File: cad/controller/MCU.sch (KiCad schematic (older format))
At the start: 37 parts, among them J3 Conn_02x03_Odd_Even, J4 Conn_01x02, J5 Conn_01x04, J6 Conn_01x05, J7 6P6C, SW2 SW_Push, U5 ATmega328-PU, U6 PCA9517A, U7 TXB0104D, Y2 18MHz

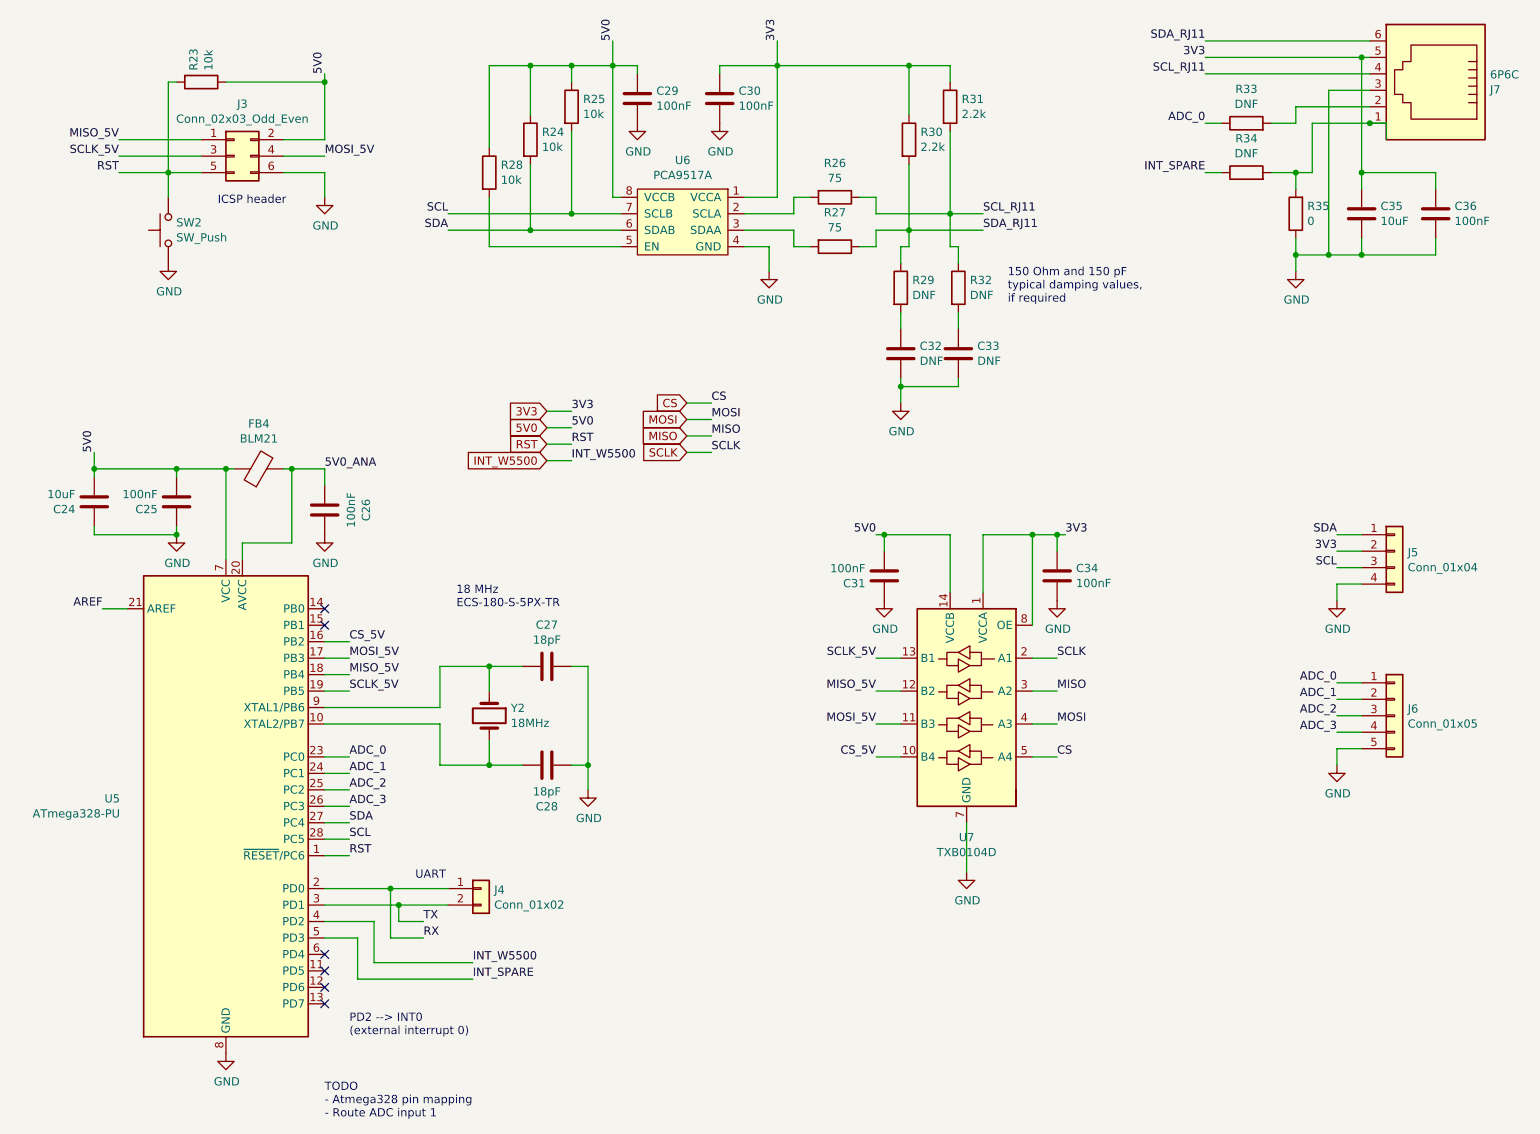
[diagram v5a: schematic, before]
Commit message: added debug dir
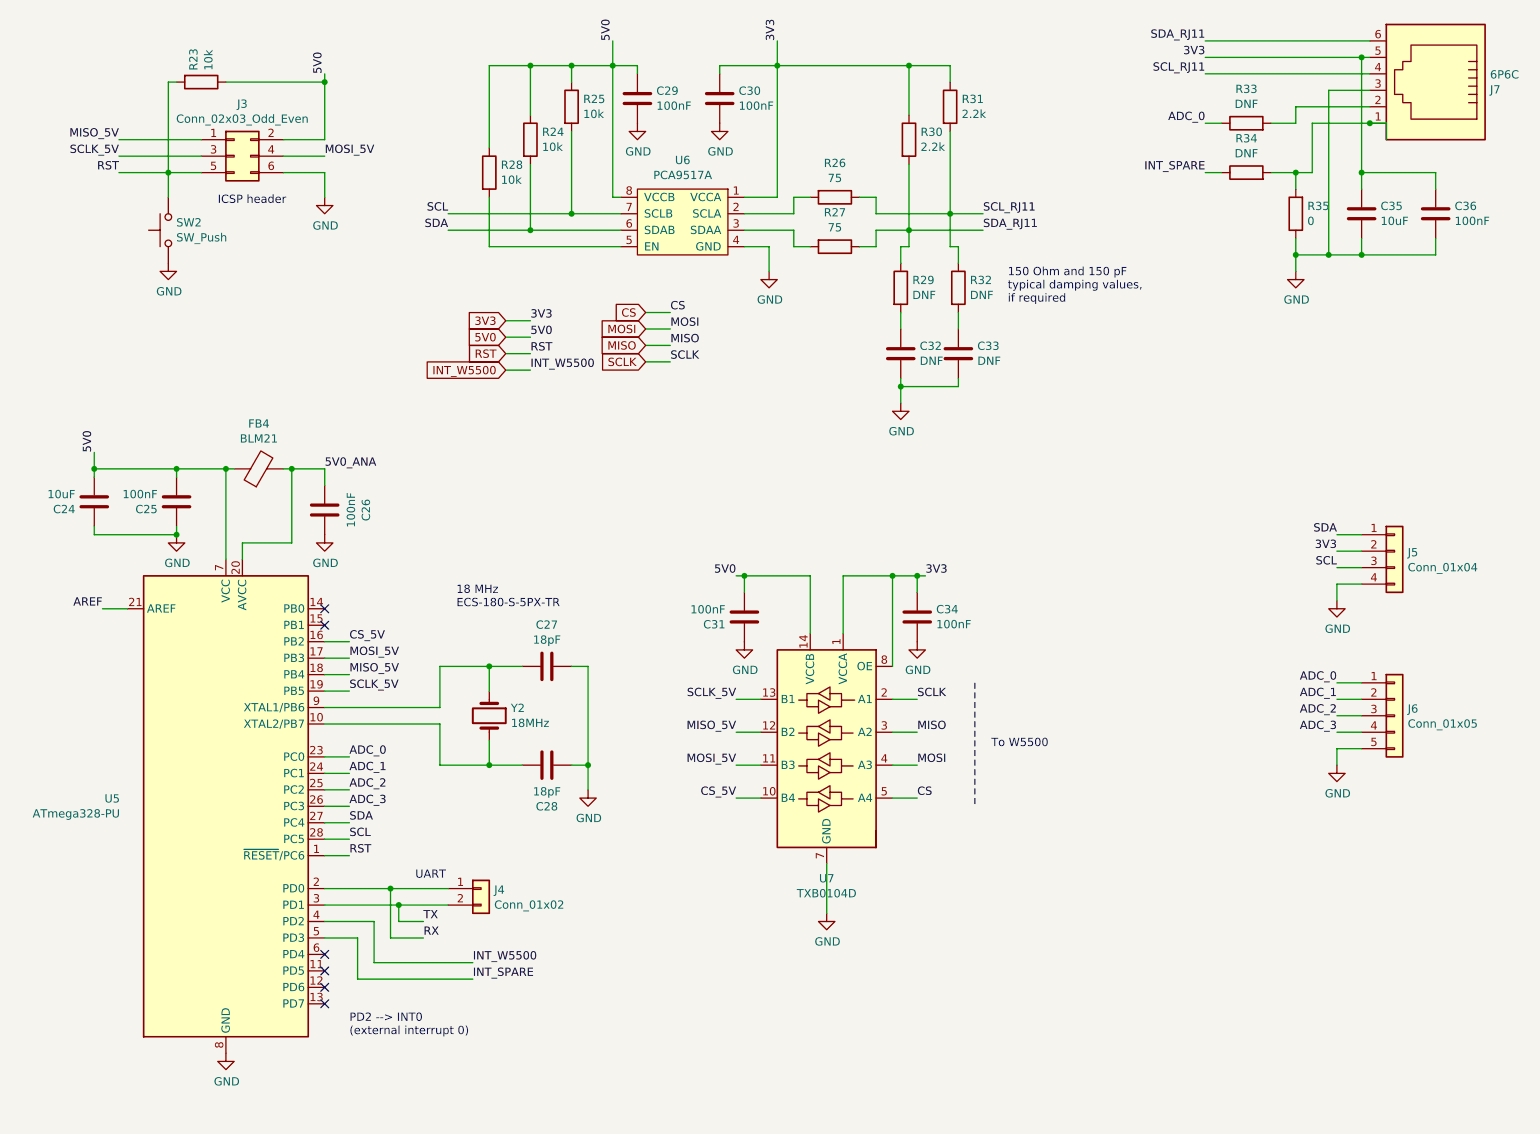
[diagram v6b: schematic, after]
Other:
- note added: "To W5500"
- note removed: "TODO\n- Atmega328 pin mapping\n- Route ADC input 1"
- moved on the sheet: C31, C34, U7
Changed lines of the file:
@@
 Text Notes 3550 4350 0    50   ~ 0
 18 MHz\nECS-180-S-5PX-TR
-Text Notes 2750 7450 0    50   ~ 0
-TODO\n- Atmega328 pin mapping\n- Route ADC input 1
 $Comp
 L Logic_LevelTranslator:TXB0104D U7
 U 1 1 62D75B44
-P 6650 4950
-F 0 "U7" H 6650 4161 50  0000 C CNN
-F 1 "TXB0104D" H 6650 4070 50  0000 C CNN
-F 2 "Package_SO:SOIC-14_3.9x8.7mm_P1.27mm" H 6650 4200 50  0001 C CNN
-F 3 "http://www.ti.com/lit/ds/symlink/txb0104.pdf" H 6760 5045 50  0001 C CNN
-	1    6650 4950
+P 5800 5200
+F 0 "U7" H 5800 4411 50  0000 C CNN
+F 1 "TXB0104D" H 5800 4320 50  0000 C CNN
+F 2 "Package_SO:SOIC-14_3.9x8.7mm_P1.27mm" H 5800 4450 50  0001 C CNN
+F 3 "http://www.ti.com/lit/ds/symlink/txb0104.pdf" H 5910 5295 50  0001 C CNN
+	1    5800 5200
 	-1   0    0    -1
 $EndComp
-Text Label 6100 3900 2    50   ~ 0
+Text Label 5250 4150 2    50   ~ 0
 5V0
-Text Label 7250 3900 0    50   ~ 0
+Text Label 6400 4150 0    50   ~ 0
 3V3
 Wire Wire Line
-	6250 4650 6100 4650
-Wire Wire Line
-	6250 5050 6100 5050
-Wire Wire Line
-	6250 5250 6100 5250
-Text Label 6100 4650 2    50   ~ 0
+	5400 4900 5250 4900
+Wire Wire Line
+	5400 5300 5250 5300
+Wire Wire Line
+	5400 5500 5250 5500
+Text Label 5250 4900 2    50   ~ 0
 SCLK_5V
-Text Label 6100 5250 2    50   ~ 0
+Text Label 5250 5500 2    50   ~ 0
 CS_5V
-Text Label 6100 5050 2    50   ~ 0
+Text Label 5250 5300 2    50   ~ 0
 MOSI_5V
-Text Label 6100 4850 2    50   ~ 0
+Text Label 5250 5100 2    50   ~ 0
 MISO_5V
 Wire Wire Line
-	6250 4850 6100 4850
-Wire Wire Line
-	7050 5050 7200 5050
-Wire Wire Line
-	7050 4650 7200 4650
-Wire Wire Line
-	7050 5250 7200 5250
-Text Label 7200 4650 0    50   ~ 0
+	5400 5100 5250 5100
+Wire Wire Line
+	6200 5300 6350 5300
+Wire Wire Line
+	6200 4900 6350 4900
+Wire Wire Line
+	6200 5500 6350 5500
+Text Label 6350 4900 0    50   ~ 0
 SCLK
-Text Label 7200 5250 0    50   ~ 0
+Text Label 6350 5500 0    50   ~ 0
 CS
-Text Label 7200 5050 0    50   ~ 0
+Text Label 6350 5300 0    50   ~ 0
 MOSI
-Text Label 7200 4850 0    50   ~ 0
+Text Label 6350 5100 0    50   ~ 0
 MISO
 Wire Wire Line
-	7050 4850 7200 4850
+	6200 5100 6350 5100
 Wire Wire Line
 	9050 1000 9050 1700
@@
 L Device:C C34
 U 1 1 631DB87C
-P 7200 4150
-F 0 "C34" H 7315 4196 50  0000 L CNN
-F 1 "100nF" H 7315 4105 50  0000 L CNN
-F 2 "Capacitor_SMD:C_0603_1608Metric" H 7238 4000 50  0001 C CNN
-F 3 "~" H 7200 4150 50  0001 C CNN
-	1    7200 4150
+P 6350 4400
+F 0 "C34" H 6465 4446 50  0000 L CNN
+F 1 "100nF" H 6465 4355 50  0000 L CNN
+F 2 "Capacitor_SMD:C_0603_1608Metric" H 6388 4250 50  0001 C CNN
+F 3 "~" H 6350 4400 50  0001 C CNN
+	1    6350 4400
 	1    0    0    -1
 $EndComp
@@
 L Device:C C31
 U 1 1 631DFFCE
-P 6150 4150
-F 0 "C31" H 6265 4196 50  0000 L CNN
-F 1 "100nF" H 6265 4105 50  0000 L CNN
-F 2 "Capacitor_SMD:C_0603_1608Metric" H 6188 4000 50  0001 C CNN
-F 3 "~" H 6150 4150 50  0001 C CNN
-	1    6150 4150
+P 5300 4400
+F 0 "C31" H 5415 4446 50  0000 L CNN
+F 1 "100nF" H 5415 4355 50  0000 L CNN
+F 2 "Capacitor_SMD:C_0603_1608Metric" H 5338 4250 50  0001 C CNN
+F 3 "~" H 5300 4400 50  0001 C CNN
+	1    5300 4400
 	-1   0    0    1
 $EndComp
@@
 L power:GND #PWR036
 U 1 1 63218CA3
-P 7200 4300
-F 0 "#PWR036" H 7200 4050 50  0001 C CNN
-F 1 "GND" H 7205 4127 50  0000 C CNN
-F 2 "" H 7200 4300 50  0001 C CNN
-F 3 "" H 7200 4300 50  0001 C CNN
-	1    7200 4300
+P 6350 4550
+F 0 "#PWR036" H 6350 4300 50  0001 C CNN
+F 1 "GND" H 6355 4377 50  0000 C CNN
+F 2 "" H 6350 4550 50  0001 C CNN
+F 3 "" H 6350 4550 50  0001 C CNN
+	1    6350 4550
 	1    0    0    -1
 $EndComp
@@
 L power:GND #PWR034
 U 1 1 632191F1
-P 6150 4300
-F 0 "#PWR034" H 6150 4050 50  0001 C CNN
-F 1 "GND" H 6155 4127 50  0000 C CNN
-F 2 "" H 6150 4300 50  0001 C CNN
-F 3 "" H 6150 4300 50  0001 C CNN
-	1    6150 4300
-	1    0    0    -1
-$EndComp
-Wire Wire Line
-	7200 4000 7200 3900
-Connection ~ 7200 3900
-Wire Wire Line
-	7200 3900 7250 3900
-Wire Wire Line
-	6150 4000 6150 3900
-Wire Wire Line
-	6100 3900 6150 3900
-Connection ~ 6150 3900
+P 5300 4550
+F 0 "#PWR034" H 5300 4300 50  0001 C CNN
+F 1 "GND" H 5305 4377 50  0000 C CNN
+F 2 "" H 5300 4550 50  0001 C CNN
+F 3 "" H 5300 4550 50  0001 C CNN
+	1    5300 4550
+	1    0    0    -1
+$EndComp
+Wire Wire Line
+	6350 4250 6350 4150
+Connection ~ 6350 4150
+Wire Wire Line
+	6350 4150 6400 4150
+Wire Wire Line
+	5300 4250 5300 4150
+Wire Wire Line
+	5250 4150 5300 4150
+Connection ~ 5300 4150
 $Comp
 L Device:Ferrite_Bead FB4
@@
 Connection ~ 1350 3500
 Wire Wire Line
-	6550 4250 6550 3900
-Wire Wire Line
-	6150 3900 6550 3900
-Wire Wire Line
-	6750 4250 6750 3900
-Wire Wire Line
-	6750 3900 7050 3900
+	5700 4500 5700 4150
+Wire Wire Line
+	5300 4150 5700 4150
+Wire Wire Line
+	5900 4500 5900 4150
+Wire Wire Line
+	5900 4150 6200 4150
 $Comp
 L Device:C C35
@@
 Text Notes 6900 2500 0    50   ~ 0
 150 Ohm and 150 pF\ntypical damping values,\nif required
-Text GLabel 4100 3150 0    50   Input ~ 0
+Text GLabel 3850 2600 0    50   Input ~ 0
 3V3
-Text Label 4250 3150 0    50   ~ 0
+Text Label 4000 2600 0    50   ~ 0
 3V3
 Wire Wire Line
-	4100 3150 4250 3150
-Text GLabel 4100 3250 0    50   Input ~ 0
+	3850 2600 4000 2600
+Text GLabel 3850 2700 0    50   Input ~ 0
 5V0
-Text Label 4250 3250 0    50   ~ 0
+Text Label 4000 2700 0    50   ~ 0
 5V0
 Wire Wire Line
-	4100 3250 4250 3250
-Text Label 5100 3400 0    50   ~ 0
+	3850 2700 4000 2700
+Text Label 4850 2850 0    50   ~ 0
 SCLK
-Text Label 5100 3300 0    50   ~ 0
+Text Label 4850 2750 0    50   ~ 0
 MISO
-Text Label 5100 3200 0    50   ~ 0
+Text Label 4850 2650 0    50   ~ 0
 MOSI
-Text Label 5100 3100 0    50   ~ 0
+Text Label 4850 2550 0    50   ~ 0
 CS
-Text GLabel 4950 3100 0    50   Input ~ 0
+Text GLabel 4700 2550 0    50   Input ~ 0
 CS
-Text GLabel 4950 3200 0    50   Input ~ 0
+Text GLabel 4700 2650 0    50   Input ~ 0
 MOSI
-Text GLabel 4950 3300 0    50   Input ~ 0
+Text GLabel 4700 2750 0    50   Input ~ 0
 MISO
-Text GLabel 4950 3400 0    50   Input ~ 0
+Text GLabel 4700 2850 0    50   Input ~ 0
 SCLK
 Wire Wire Line
-	4950 3100 5100 3100
-Wire Wire Line
-	4950 3200 5100 3200
-Wire Wire Line
-	4950 3300 5100 3300
-Wire Wire Line
-	4950 3400 5100 3400
-Wire Wire Line
-	6650 5650 6650 5950
+	4700 2550 4850 2550
+Wire Wire Line
+	4700 2650 4850 2650
+Wire Wire Line
+	4700 2750 4850 2750
+Wire Wire Line
+	4700 2850 4850 2850
+Wire Wire Line
+	5800 5900 5800 6200
 $Comp
 L power:GND #PWR0102
 U 1 1 62DBDB96
-P 6650 5950
-F 0 "#PWR0102" H 6650 5700 50  0001 C CNN
-F 1 "GND" H 6655 5777 50  0000 C CNN
-F 2 "" H 6650 5950 50  0001 C CNN
-F 3 "" H 6650 5950 50  0001 C CNN
-	1    6650 5950
-	1    0    0    -1
-$EndComp
-Text Label 4250 3350 0    50   ~ 0
+P 5800 6200
+F 0 "#PWR0102" H 5800 5950 50  0001 C CNN
+F 1 "GND" H 5805 6027 50  0000 C CNN
+F 2 "" H 5800 6200 50  0001 C CNN
+F 3 "" H 5800 6200 50  0001 C CNN
+	1    5800 6200
+	1    0    0    -1
+$EndComp
+Text Label 4000 2800 0    50   ~ 0
 RST
-Text GLabel 4100 3350 0    50   Input ~ 0
+Text GLabel 3850 2800 0    50   Input ~ 0
 RST
 Wire Wire Line
-	4100 3350 4250 3350
-Text Label 4250 3450 0    50   ~ 0
+	3850 2800 4000 2800
+Text Label 4000 2900 0    50   ~ 0
 INT_W5500
-Text GLabel 4100 3450 0    50   Input ~ 0
+Text GLabel 3850 2900 0    50   Input ~ 0
 INT_W5500
 Wire Wire Line
-	4100 3450 4250 3450
-Wire Wire Line
-	7050 3900 7050 4450
-Connection ~ 7050 3900
-Wire Wire Line
-	7050 3900 7200 3900
+	3850 2900 4000 2900
+Wire Wire Line
+	6200 4150 6200 4700
+Connection ~ 6200 4150
+Wire Wire Line
+	6200 4150 6350 4150
 $Comp
 L custom_digital:PCA9517A U6
@@
 Wire Wire Line
 	6100 2050 6300 2050
+Wire Notes Line
+	6700 4800 6700 5550
+Text Notes 6800 5200 0    50   ~ 0
+To W5500
 $EndSCHEMATC
